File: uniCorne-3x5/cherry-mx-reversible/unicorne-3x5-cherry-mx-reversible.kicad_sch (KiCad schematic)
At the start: 87 parts, among them J1 MJ-4PP-9, J2 Nice!View, J3 Conn_01x02, J3 Conn_01x03, SW1 SW_MX_HS, SW10 SW_MX_HS, SW11 SW_MX_HS, SW12 SW_MX_HS, SW13 SW_MX_HS, SW14 SW_MX_HS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

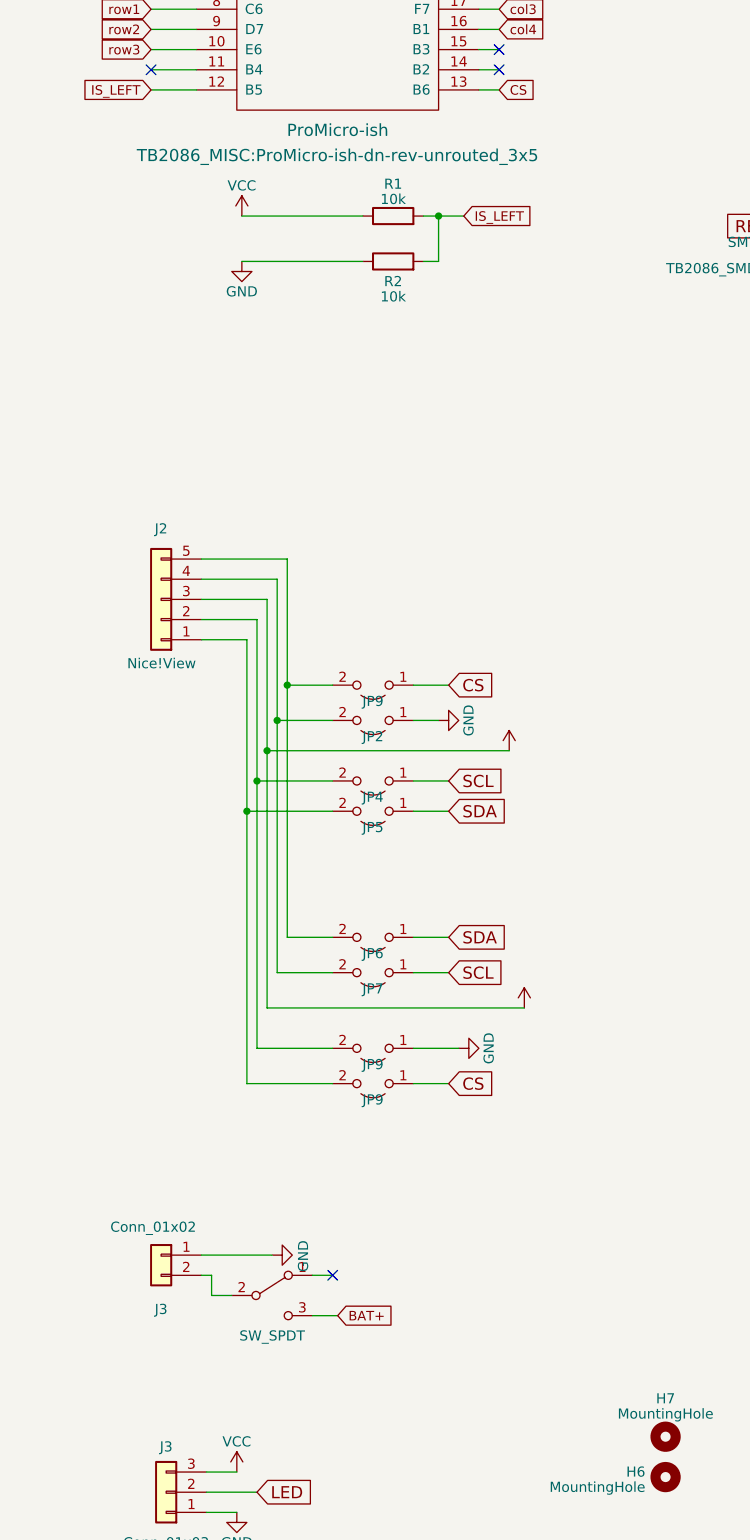
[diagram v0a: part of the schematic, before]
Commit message: amended cherry mx 3x5
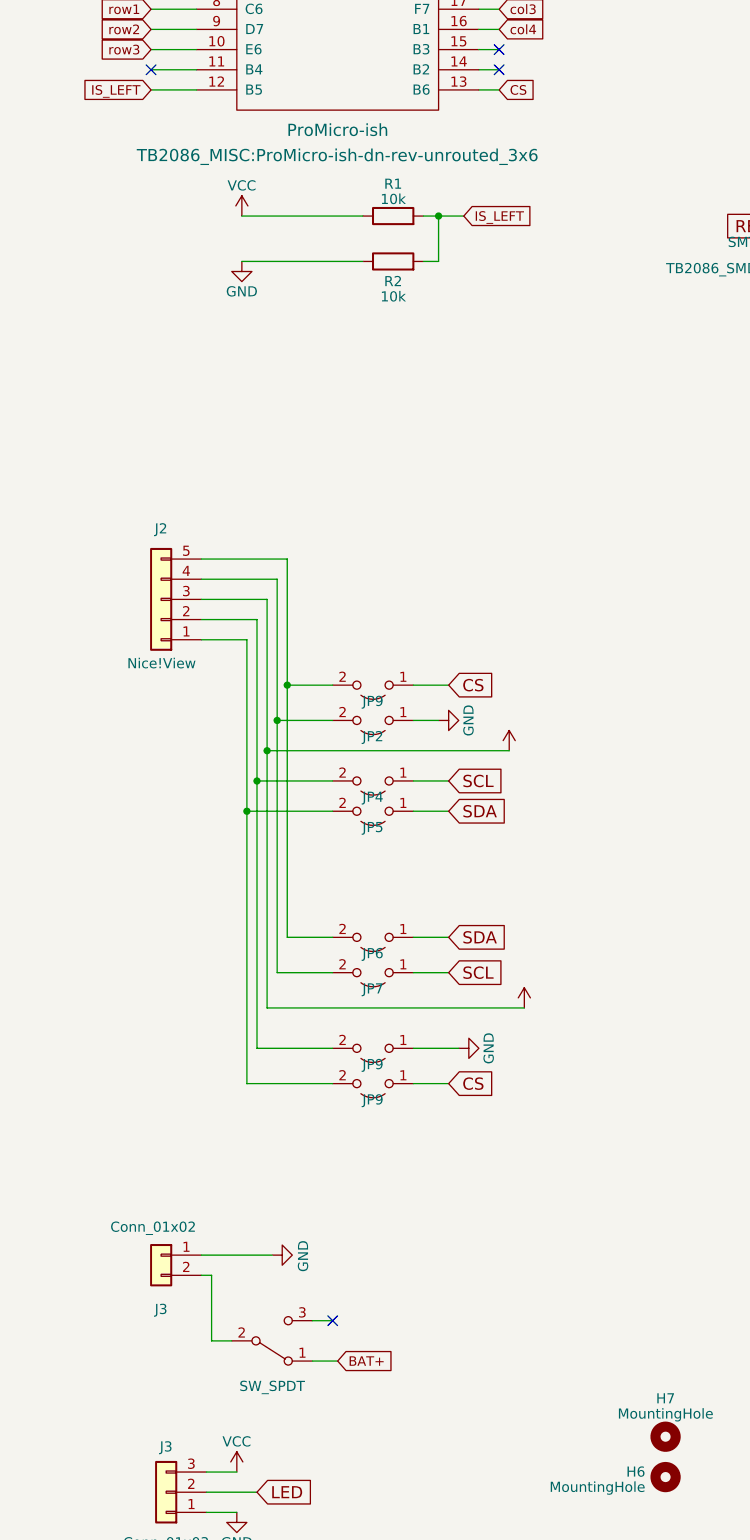
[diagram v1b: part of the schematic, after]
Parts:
- U1: footprint TB2086_MISC:ProMicro-ish-dn-rev-unrouted_3x5 -> TB2086_MISC:ProMicro-ish-dn-rev-unrouted_3x6
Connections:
- net BAT+: now also PSW1.1 (A); no longer PSW1.3 (C)

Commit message: fixed footprint for promicro-ish 3x6
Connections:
- net CS: now also U1.12 (B5); no longer U1.13 (B6)
- net IS_LEFT: now also U1.13 (B6); no longer U1.12 (B5)
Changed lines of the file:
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@@
     )
   )
-  (global_label "CS" (shape input) (at 80.645 54.61 0) (fields_autoplaced)
+  (global_label "IS_LEFT" (shape input) (at 80.645 54.61 0) (fields_autoplaced)
     (effects (font (size 1.1938 1.1938)) (justify left))
-    (property "Intersheetrefs" "${INTERSHEET_REFS}" (at 85.7069 54.61 0)
+    (property "Intersheetrefs" "${INTERSHEET_REFS}" (at 89.9706 54.61 0)
       (effects (font (size 1.27 1.27)) (justify left) hide)
     )
@@
     )
   )
-  (global_label "IS_LEFT" (shape input) (at 36.83 54.61 180) (fields_autoplaced)
+  (global_label "CS" (shape input) (at 36.83 54.61 180) (fields_autoplaced)
     (effects (font (size 1.1938 1.1938)) (justify right))
-    (property "Intersheetrefs" "${INTERSHEET_REFS}" (at 27.5044 54.61 0)
+    (property "Intersheetrefs" "${INTERSHEET_REFS}" (at 31.7681 54.61 0)
       (effects (font (size 1.27 1.27)) (justify right) hide)
     )

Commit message: fixed 3x5
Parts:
- removed JP9: Jumper_3_Bridged12, TB2086_MISC:SolderJumper-3_P1.3mm_Bridged2Bar12_RoundedPad1.0x1.5mm_rev, symbol Jumper:Jumper_3_Bridged12
- added JP10: Jumper_3_Bridged12, TB2086_MISC:SolderJumper-3_P1.3mm_Bridged2Bar12_RoundedPad1.0x1.5mm_rev, symbol Jumper:Jumper_3_Bridged12
- added JP11, JP9: (no value), TB2086_MISC:SolderJumper-2_P1.3mm_Open_TrianglePad1.0x1.2mm_rev, symbol Jumper:Jumper_2_Open
- U1: footprint TB2086_MISC:ProMicro-ish-dn-rev-unrouted_3x6 -> TB2086_MISC:ProMicro-ish-dn-rev-unrouted_3x5
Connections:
- net BAT+: now also U1.24 (RAW)
- net DATA: now also JP10.1 (A)
- net GND: now also JP11.2 (B); no longer U1.26 (GND)
- net SCL: now also JP9.1 (A); no longer J1.A
- net SDA: now also JP10.3 (B)
- net at J1.B: now also JP10.2 (C)
- new net: J1.A, JP9.2 (B)
- new net B-/D-: JP11.1 (A), U1.26 (B-/D-)
- no-connect marks 6 -> 5

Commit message: KiCAD 8
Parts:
- JP11, JP2, JP4, JP5, JP6, JP7, JP9: value (none) -> (none)
